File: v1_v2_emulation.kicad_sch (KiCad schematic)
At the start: 8 parts, among them CN5 LED, IC20 7407, IC65 D65101GD110

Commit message: fix pitch of IC65 pads
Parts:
- IC65: footprint 88va_Library:QFP-160_28x28_Pitch0.635mm -> 88va_Library:QFP-160_27.8x27.8_Pitch0.65mm
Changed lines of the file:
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@@
       (effects (font (size 1.27 1.27)) (justify left))
     )
-    (property "Footprint" "88va_Library:QFP-160_28x28_Pitch0.635mm" (at 137.16 72.39 0)
+    (property "Footprint" "88va_Library:QFP-160_27.8x27.8_Pitch0.65mm" (at 137.16 72.39 0)
       (effects (font (size 1.27 1.27)) hide)
     )

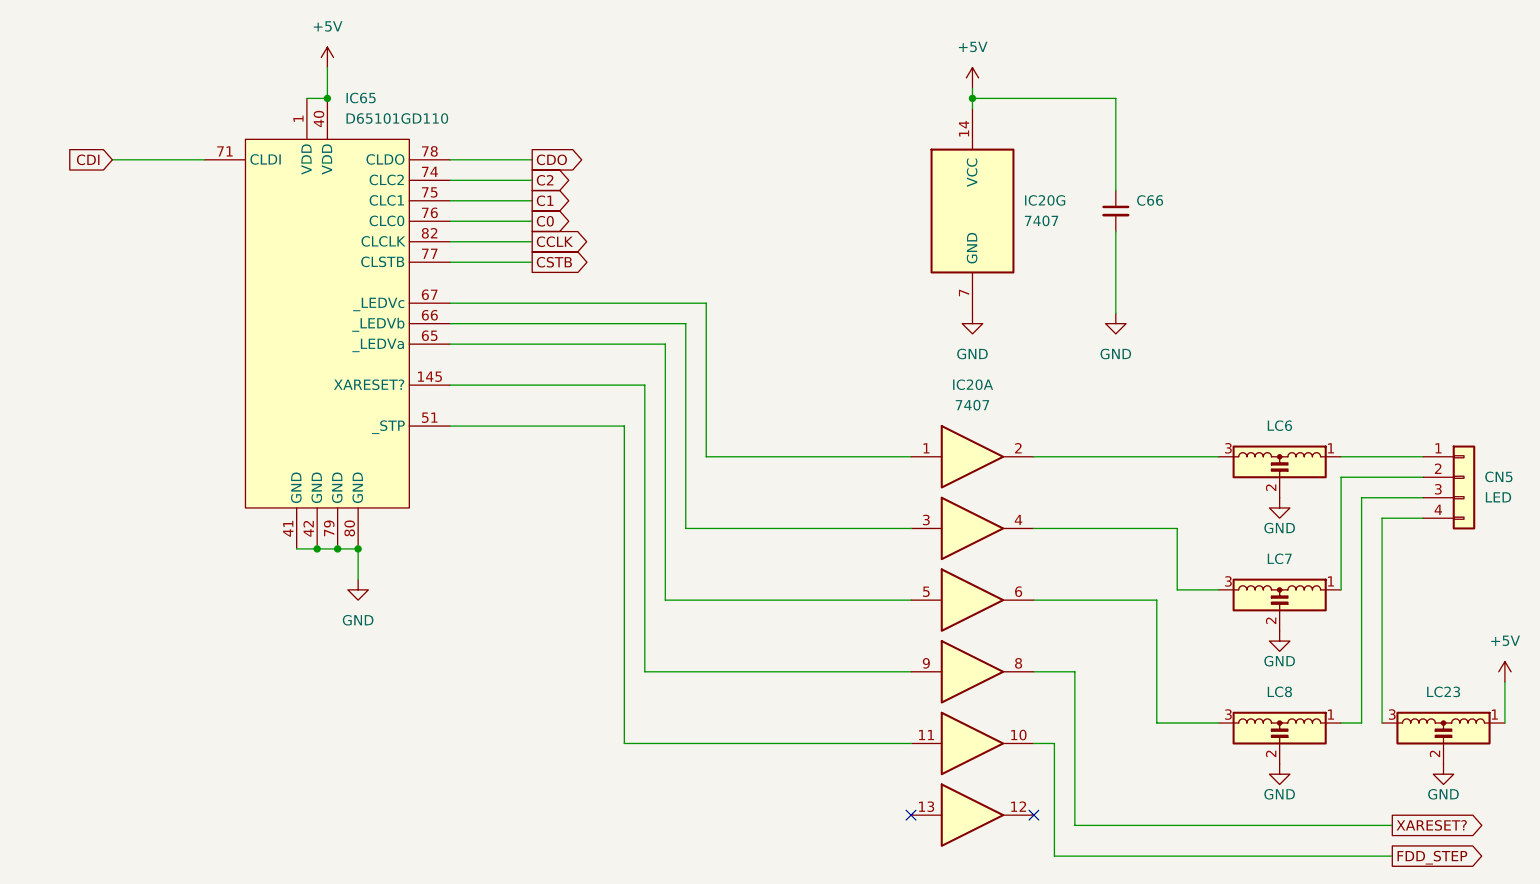
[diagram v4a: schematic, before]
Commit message: add display clock generator
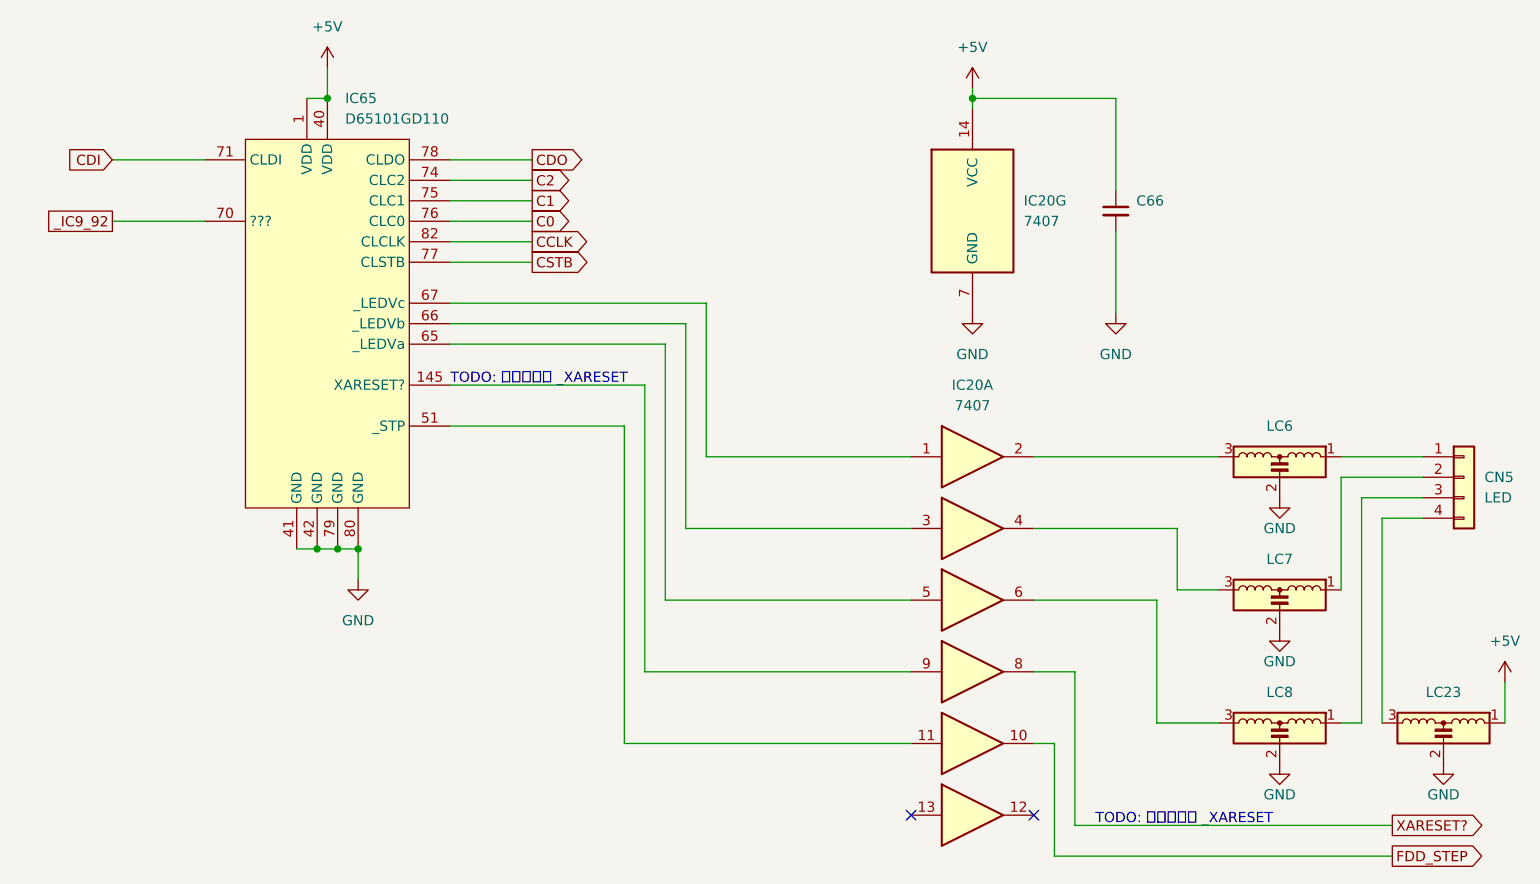
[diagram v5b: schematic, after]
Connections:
- new net _IC9_92: IC65.70 (???)
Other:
- note added: "TODO: 名称を変更 _XARESET"
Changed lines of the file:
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@@
+    (stroke (width 0) (type default))
+  )
+  (wire (pts (xy 110.49 85.09) (xy 121.92 85.09))
     (stroke (width 0) (type default))
   )
@@
   (wire (pts (xy 224.79 123.19) (xy 242.57 123.19))
     (stroke (width 0) (type default))
+  )
+  (text "TODO: 名称を変更 _XARESET" (at 152.4 105.41 0)
+    (effects (font (size 1.27 1.27)) (justify left bottom))
+  )
+  (text "TODO: 名称を変更 _XARESET" (at 232.41 160.02 0)
+    (effects (font (size 1.27 1.27)) (justify left bottom))
   )
   (global_label "XARESET?" (shape output) (at 269.24 160.02 0) (fields_autoplaced)
@@
     (property "Intersheetrefs" "${INTERSHEET_REFS}" (at 169.4157 77.47 0)
       (effects (font (size 1.27 1.27)) (justify left) hide)
+    )
+  )
+  (global_label "_IC9_92" (shape passive) (at 110.49 85.09 180) (fields_autoplaced)
+    (effects (font (size 1.27 1.27)) (justify right))
+    (property "Intersheetrefs" "${INTERSHEET_REFS}" (at 101.1776 85.09 0)
+      (effects (font (size 1.27 1.27)) (justify right) hide)
     )
   )
@@
     (pin "145")
     (pin "67")
+    (pin "70")
     (instances
       (project "88va2-circuit"

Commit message: fix errors
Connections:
- net XARESET? renamed _XARESET
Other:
- note removed: "TODO: 名称を変更 _XARESET"
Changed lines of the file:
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@@
     (stroke (width 0) (type default))
   )
-  (text "TODO: 名称を変更 _XARESET" (at 152.4 105.41 0)
-    (effects (font (size 1.27 1.27)) (justify left bottom))
-  )
-  (text "TODO: 名称を変更 _XARESET" (at 232.41 160.02 0)
-    (effects (font (size 1.27 1.27)) (justify left bottom))
-  )
-  (global_label "XARESET?" (shape output) (at 269.24 160.02 0) (fields_autoplaced)
+  (global_label "_XARESET" (shape output) (at 269.24 160.02 0) (fields_autoplaced)
     (effects (font (size 1.27 1.27)) (justify left))
-    (property "Intersheetrefs" "${INTERSHEET_REFS}" (at 281.357 160.02 0)
+    (property "Intersheetrefs" "${INTERSHEET_REFS}" (at 281.236 160.02 0)
       (effects (font (size 1.27 1.27)) (justify left) hide)
     )

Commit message: schematic: tidy hierarchical sheets
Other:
- title: (none) -> V1/V2モード エミュレータ
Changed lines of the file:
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@@
 (kicad_sch (version 20230121) (generator eeschema)
   (paper "A4")
+  (title_block
+    (title "V1/V2モード エミュレータ")
+    (comment 1 "VA1回路図 P.250")
+  )
   (junction (at 135.89 125.73) (diameter 0) (color 0 0 0 0)
   )
